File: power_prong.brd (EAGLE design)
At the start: 49.8 x 11.8 mm, 19 parts, among them IC1 INA138, IC2 MCP1824S, Q1 FDG332PZ, X1 USBSMD

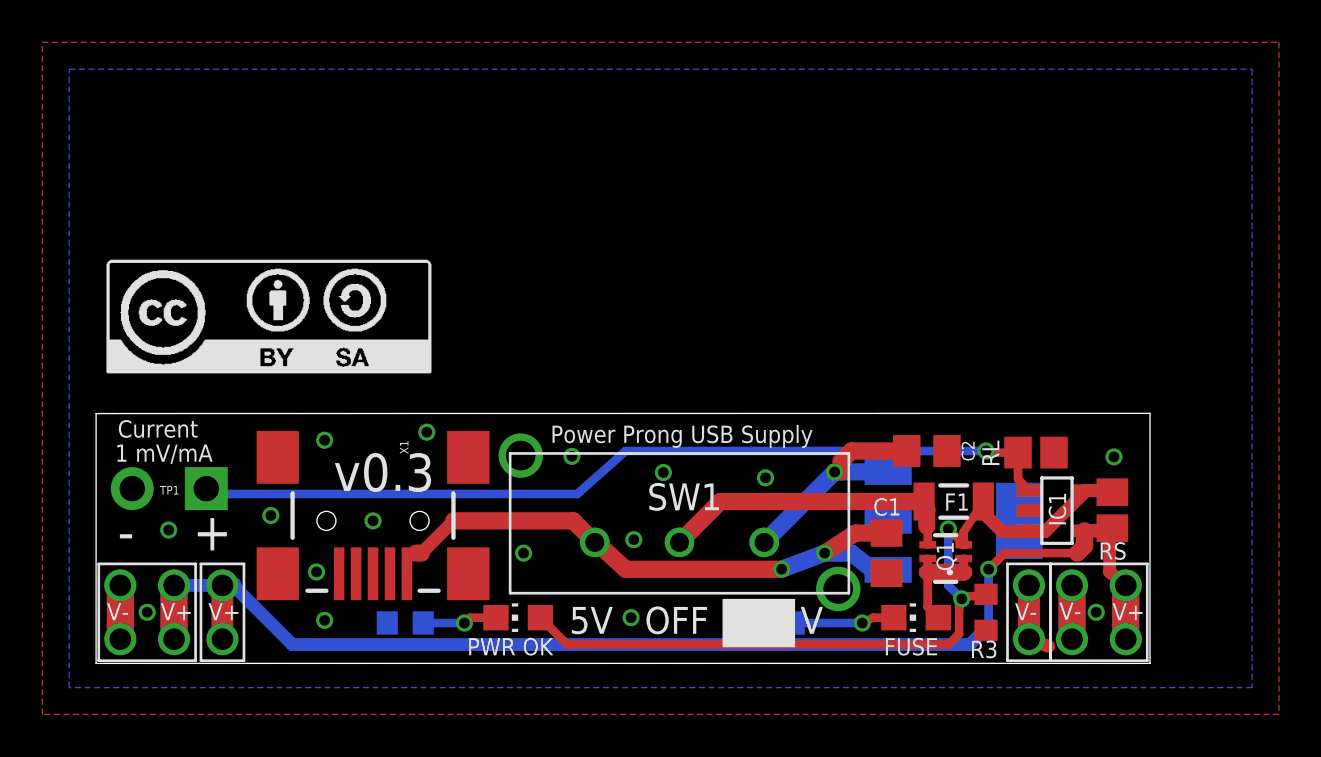
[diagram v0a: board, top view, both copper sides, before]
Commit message: Resize for panelizing
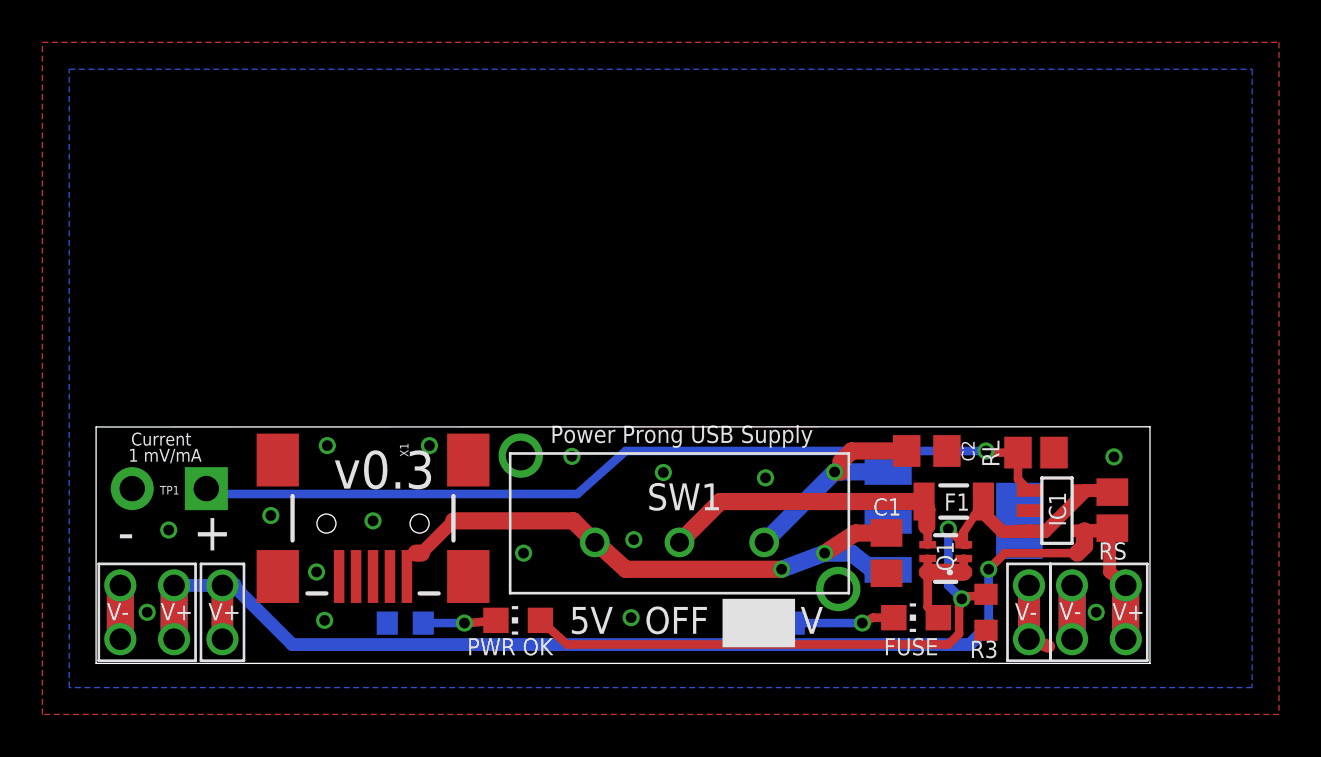
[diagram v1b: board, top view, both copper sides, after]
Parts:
- removed LOGO1: LOGO_CC-BY-SA, dp_devices:CC-BY-SA
- moved PWR_OK 0.13 mm to (19.9, 1.91)
- moved X1 0.13 mm to (13.1, 6.48)
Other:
- board size 49.8 x 11.8 mm -> 49.8 x 11.2 mm
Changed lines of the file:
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@@
 <layer number="23" name="tOrigins" color="15" fill="1" visible="yes" active="yes"/>
 <layer number="24" name="bOrigins" color="15" fill="1" visible="yes" active="yes"/>
-<layer number="25" name="tNames" color="7" fill="1" visible="yes" active="yes"/>
-<layer number="26" name="bNames" color="7" fill="1" visible="yes" active="yes"/>
+<layer number="25" name="tNames" color="7" fill="1" visible="no" active="yes"/>
+<layer number="26" name="bNames" color="7" fill="1" visible="no" active="yes"/>
 <layer number="27" name="tValues" color="7" fill="1" visible="no" active="yes"/>
 <layer number="28" name="bValues" color="7" fill="1" visible="no" active="yes"/>
@@
 <layer number="50" name="dxf" color="7" fill="1" visible="no" active="no"/>
 <layer number="51" name="tDocu" color="6" fill="1" visible="yes" active="yes"/>
-<layer number="52" name="bDocu" color="7" fill="1" visible="yes" active="yes"/>
+<layer number="52" name="bDocu" color="7" fill="1" visible="no" active="yes"/>
 <layer number="53" name="tGND_GNDA" color="7" fill="9" visible="no" active="no"/>
 <layer number="54" name="bGND_GNDA" color="1" fill="9" visible="no" active="no"/>
@@
 <plain>
 <wire x1="0" y1="-0.127" x2="49.784" y2="-0.127" width="0" layer="20"/>
-<wire x1="49.784" y1="-0.127" x2="49.784" y2="11.684" width="0" layer="20"/>
-<wire x1="49.784" y1="11.684" x2="0" y2="11.674" width="0" layer="20"/>
-<wire x1="0" y1="11.674" x2="0" y2="-0.127" width="0" layer="20"/>
+<wire x1="49.784" y1="-0.127" x2="49.784" y2="11.049" width="0" layer="20"/>
+<wire x1="49.784" y1="11.049" x2="0" y2="11.039" width="0" layer="20"/>
+<wire x1="0" y1="11.039" x2="0" y2="-0.127" width="0" layer="20"/>
 <text x="4.572" y="5.207" size="1.778" layer="21" font="vector" ratio="15">+</text>
 <text x="1.016" y="5.207" size="1.778" layer="21" font="vector" ratio="15">-</text>
-<text x="1.016" y="10.541" size="0.8128" layer="21" font="vector" ratio="15">Current</text>
-<text x="0.889" y="9.398" size="0.8128" layer="21" font="vector" ratio="15">1 mV/mA</text>
+<text x="1.651" y="10.16" size="0.6096" layer="21" font="vector" ratio="15">Current</text>
+<text x="1.524" y="9.398" size="0.6096" layer="21" font="vector" ratio="15">1 mV/mA</text>
 <text x="37.211" y="0.254" size="0.8128" layer="21" font="vector" ratio="15">FUSE</text>
 <text x="17.526" y="0.254" size="0.8128" layer="21" font="vector" ratio="15">PWR OK</text>
-<text x="16.002" y="9.779" size="1.778" layer="21" font="vector" ratio="15" rot="R180">v0.3</text>
+<text x="16.002" y="9.906" size="1.778" layer="21" font="vector" ratio="15" rot="R180">v0.3</text>
 <text x="31.75" y="2.794" size="1.4224" layer="22" font="vector" ratio="15" rot="MR0">Space Age Robotics</text>
-<text x="36.957" y="9.906" size="1.016" layer="22" font="vector" ratio="15" rot="MR0">Andrew Schamp</text>
-<text x="6.096" y="10.16" size="0.8128" layer="22" font="vector" ratio="15" rot="MR0">20120823</text>
-<text x="9.144" y="10.16" size="0.8128" layer="22" font="vector" ratio="15" rot="MR0">v0.3</text>
+<text x="35.814" y="9.652" size="1.016" layer="22" font="vector" ratio="15" rot="MR0">Andrew Schamp</text>
+<text x="6.096" y="9.906" size="0.8128" layer="22" font="vector" ratio="15" rot="MR0">20120823</text>
+<text x="9.144" y="9.906" size="0.8128" layer="22" font="vector" ratio="15" rot="MR0">v0.3</text>
 <rectangle x1="29.591" y1="0.635" x2="33.02" y2="2.921" layer="21"/>
 <text x="22.352" y="1.27" size="1.27" layer="21" font="vector" ratio="15">5V</text>
@@
 <attribute name="VALUE" x="40.005" y="4.572" size="1.27" layer="27" rot="R180"/>
 </element>
-<element name="PWR_OK" library="led" package="CHIP-LED0805" value="" x="19.939" y="2.032" smashed="yes" rot="R90">
-<attribute name="VALUE" x="21.209" y="4.572" size="1.27" layer="27" rot="R180"/>
+<element name="PWR_OK" library="led" package="CHIP-LED0805" value="" x="19.939" y="1.905" smashed="yes" rot="R90">
+<attribute name="VALUE" x="21.209" y="4.445" size="1.27" layer="27" rot="R180"/>
 </element>
 <element name="R1" library="resistor" package="R0603" value="390" x="32.131" y="1.778" smashed="yes" rot="MR180">
@@
 <attribute name="VALUE" x="38.989" y="5.8674" size="0.4064" layer="27"/>
 </element>
-<element name="X1" library="SparkFun-Connectors" package="USB-MINIB" value="USBSMD" x="13.081" y="6.604" rot="R270"/>
+<element name="X1" library="SparkFun-Connectors" package="USB-MINIB" value="USBSMD" x="13.081" y="6.477" rot="R270"/>
 <element name="RL" library="resistor" package="R0805" value="100K 1%" x="44.3992" y="9.8298" smashed="yes" rot="R180">
 <attribute name="NAME" x="42.672" y="9.144" size="0.8128" layer="25" rot="R90"/>
@@
 <attribute name="VALUE" x="6.477" y="6.858" size="0.4064" layer="27" rot="R180"/>
 </element>
-<element name="LOGO1" library="dp_devices" package="CC-BY-SA" value="LOGO_CC-BY-SA" x="0.508" y="13.589"/>
 </elements>
 <signals>
@@
 <contactref element="PWR_OK" pad="C"/>
 <contactref element="R2" pad="2"/>
-<wire x1="18.889" y1="2.032" x2="17.653" y2="2.032" width="0.4064" layer="1"/>
-<wire x1="17.653" y1="2.032" x2="17.399" y2="1.778" width="0.4064" layer="1"/>
+<wire x1="18.889" y1="1.905" x2="17.653" y2="1.778" width="0.4064" layer="1"/>
+<wire x1="17.653" y1="1.778" x2="17.399" y2="1.778" width="0.4064" layer="1"/>
 <via x="17.399" y="1.778" extent="1-16" drill="0.508"/>
 <wire x1="17.399" y1="1.778" x2="15.455" y2="1.778" width="0.4064" layer="16"/>
@@
 <via x="26.797" y="8.89" extent="1-16" drill="0.508"/>
 <via x="22.479" y="9.652" extent="1-16" drill="0.508"/>
-<via x="15.621" y="10.795" extent="1-16" drill="0.508"/>
+<via x="15.748" y="10.16" extent="1-16" drill="0.508"/>
 <via x="13.081" y="6.604" extent="1-16" drill="0.508"/>
-<via x="10.795" y="10.414" extent="1-16" drill="0.508"/>
+<via x="10.922" y="10.16" extent="1-16" drill="0.508"/>
 <via x="8.255" y="6.858" extent="1-16" drill="0.508"/>
 <via x="10.414" y="4.191" extent="1-16" drill="0.508"/>
@@
 <via x="25.4" y="5.715" extent="1-16" drill="0.508"/>
 <via x="47.244" y="2.286" extent="1-16" drill="0.508"/>
-<wire x1="37.4142" y1="6.604" x2="37.338" y2="4.13" width="0" layer="19" extent="1-16"/>
+<wire x1="37.338" y1="4.13" x2="37.4142" y2="6.604" width="0" layer="19" extent="1-16"/>
 </signal>
 <signal name="N$4">
@@
 <wire x1="40.982" y1="5.476" x2="41.006" y2="5.476" width="0.4064" layer="1"/>
 <wire x1="40.259" y1="0.762" x2="22.259" y2="0.762" width="0.4064" layer="1"/>
-<wire x1="22.259" y1="0.762" x2="20.989" y2="2.032" width="0.4064" layer="1"/>
+<wire x1="22.259" y1="0.762" x2="20.989" y2="1.905" width="0.4064" layer="1"/>
 <wire x1="40.259" y1="0.762" x2="40.767" y2="1.27" width="0.4064" layer="1"/>
-<wire x1="40.767" y1="1.27" x2="40.767" y2="2.413" width="0.4064" layer="1"/>
-<wire x1="40.767" y1="2.413" x2="40.767" y2="2.54" width="0.4064" layer="1"/>
+<wire x1="40.767" y1="1.27" x2="40.767" y2="2.54" width="0.4064" layer="1"/>
 <wire x1="40.767" y1="2.54" x2="40.894" y2="2.921" width="0.4064" layer="1"/>
 <wire x1="40.894" y1="2.921" x2="41.275" y2="3.048" width="0.4064" layer="1"/>
@@
 <contactref element="SW1" pad="3"/>
 <contactref element="X1" pad="VBUS"/>
-<wire x1="14.681" y1="4.104" x2="14.681" y2="4.826" width="0.4064" layer="1"/>
+<wire x1="14.681" y1="3.977" x2="14.681" y2="4.826" width="0.4064" layer="1"/>
 <wire x1="15.367" y1="5.08" x2="16.891" y2="6.604" width="0.6096" layer="1"/>
 <wire x1="16.891" y1="6.604" x2="22.543" y2="6.604" width="0.8128" layer="1"/>
